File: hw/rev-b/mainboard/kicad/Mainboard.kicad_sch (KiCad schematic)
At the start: 0 parts

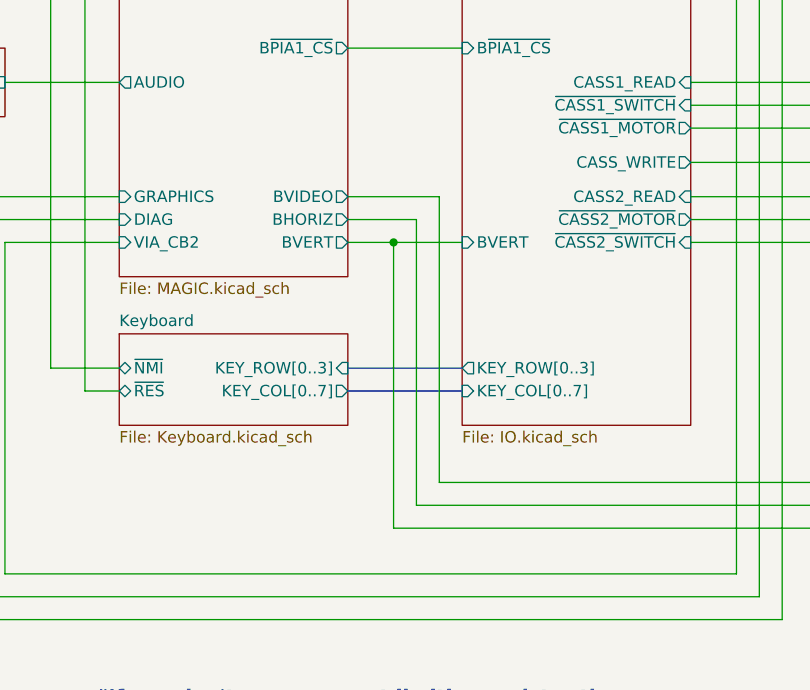
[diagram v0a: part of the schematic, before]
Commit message: hw: repurpose SP0 (spare) for independent VSYNC
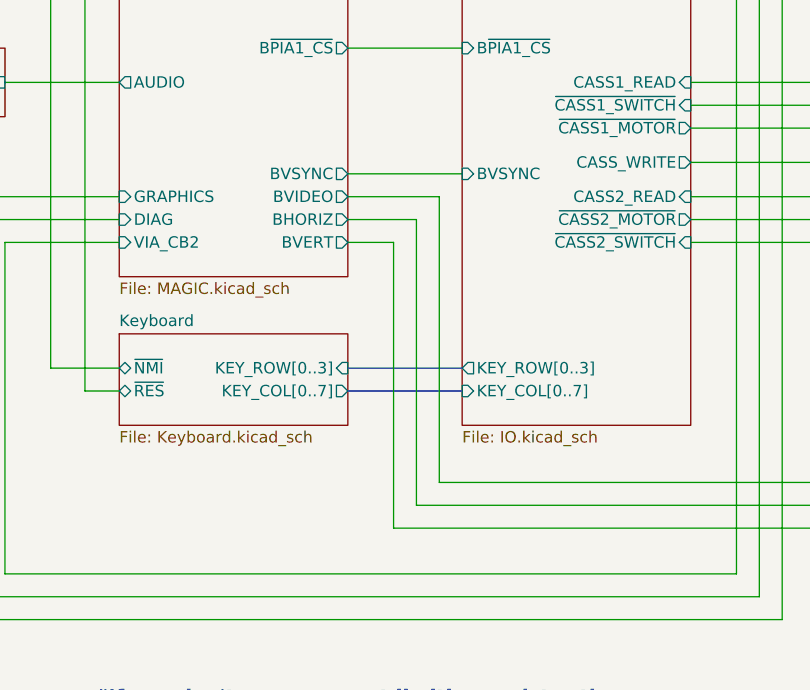
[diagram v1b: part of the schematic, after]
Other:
- sheet IO ports: added BVSYNC; removed BVERT
- sheet MAGIC ports: added BVSYNC; removed none

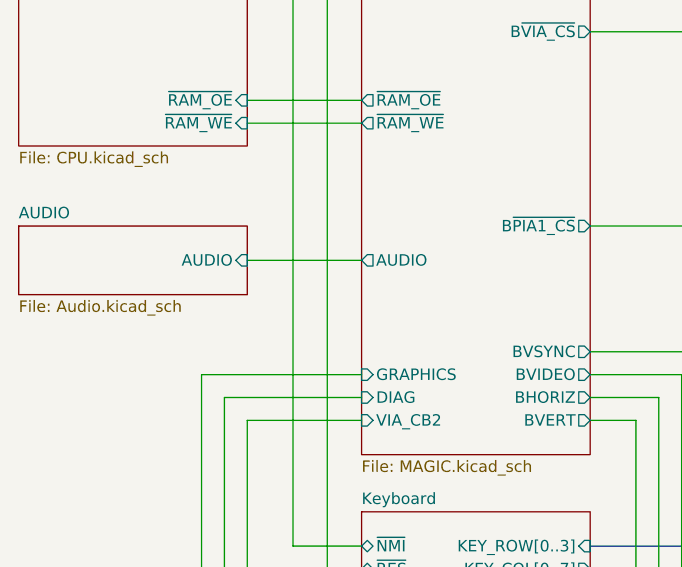
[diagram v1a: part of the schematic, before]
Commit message: hw: audio_det, stitching around sram
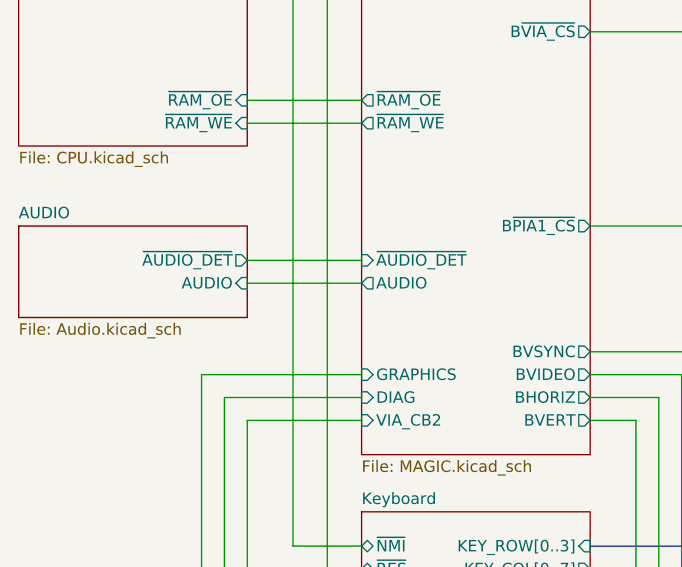
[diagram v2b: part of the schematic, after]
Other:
- sheet AUDIO ports: added ~{AUDIO_DET}; removed none
- sheet MAGIC ports: added ~{AUDIO_DET}; removed none
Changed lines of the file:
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@@
+	(wire
+		(pts
+			(xy 66.04 116.84) (xy 78.74 116.84)
+		)
+		(stroke
+			(width 0)
+			(type default)
+		)
+	)
 	(wire
 		(pts
@@
 	(wire
 		(pts
-			(xy 66.04 116.84) (xy 78.74 116.84)
-		)
-		(stroke
-			(width 0)
-			(type default)
-		)
-	)
-	(wire
-		(pts
 			(xy 66.04 60.96) (xy 78.74 60.96)
 		)
@@
 		(pts
 			(xy 168.91 69.85) (xy 142.24 69.85)
+		)
+		(stroke
+			(width 0)
+			(type default)
+		)
+	)
+	(wire
+		(pts
+			(xy 66.04 119.38) (xy 78.74 119.38)
 		)
 		(stroke
@@
 		)
 		(pin "AUDIO" output
-			(at 78.74 116.84 180)
+			(at 78.74 119.38 180)
 			(effects
 				(font
@@
 				)
 				(justify right)
+			)
+		)
+		(pin "~{AUDIO_DET}" input
+			(at 78.74 116.84 180)
+			(effects
+				(font
+					(size 1.27 1.27)
+				)
+				(justify left)
 			)
 		)
@@
 	(sheet
 		(at 40.64 113.03)
-		(size 25.4 7.62)
+		(size 25.4 10.16)
 		(fields_autoplaced yes)
 		(stroke
@@
 		)
 		(property "Sheetfile" "Audio.kicad_sch"
-			(at 40.64 121.2346 0)
+			(at 40.64 123.7746 0)
 			(effects
 				(font
@@
 		)
 		(pin "AUDIO" input
+			(at 66.04 119.38 0)
+			(effects
+				(font
+					(size 1.27 1.27)
+				)
+				(justify right)
+			)
+		)
+		(pin "~{AUDIO_DET}" output
 			(at 66.04 116.84 0)
 			(effects
